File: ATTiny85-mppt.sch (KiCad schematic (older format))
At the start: 49 parts, among them J1 S+, J2 S-, J3 O+, J4 O-, Q1 BUK9511-55A127, Q2 BUK9511-55A127, Q3 2N2222A, Q4 2N2222A, Q5 2N2907A, SW1 Write OP-AMP DIFF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

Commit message: R15 -> 4.7k. Current sensing is more higher than expected. 62mA -> 67mV.
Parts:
- D4, D8, D9: symbol 12f675-mppt-rescue:LED -> ATTiny85-mppt-rescue:LED-12f675-mppt-rescue
- L1, L2: symbol 12f675-mppt-rescue:INDUCTOR -> ATTiny85-mppt-rescue:INDUCTOR-12f675-mppt-rescue
- R15: value 10k -> 4.7k
- SW1: symbol 12f675-mppt-rescue:SW_PUSH -> ATTiny85-mppt-rescue:SW_PUSH-12f675-mppt-rescue
- U2: symbol 12f675-mppt-rescue:LM358N-RESCUE-12f675-mppt -> ATTiny85-mppt-rescue:LM358N-RESCUE-12f675-mppt-12f675-mppt-rescue
- U3: symbol MCU_Microchip_ATtiny:ATtiny85-20PU -> ATTiny85-mppt-rescue:ATtiny85-20PU-MCU_Microchip_ATtiny
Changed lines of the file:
@@
 $EndComp
 $Comp
-L 12f675-mppt-rescue:LM358N-RESCUE-12f675-mppt U2
+L ATTiny85-mppt-rescue:LM358N-RESCUE-12f675-mppt-12f675-mppt-rescue U2
 U 2 1 55C3383E
 P 7500 4850
@@
 $EndComp
 $Comp
-L 12f675-mppt-rescue:INDUCTOR L1
+L ATTiny85-mppt-rescue:INDUCTOR-12f675-mppt-rescue L1
 U 1 1 55C35536
 P 9050 2200
@@
 $EndComp
 $Comp
-L 12f675-mppt-rescue:LED D4
+L ATTiny85-mppt-rescue:LED-12f675-mppt-rescue D4
 U 1 1 55C3BFD1
 P 4550 5300
@@
 Max 25V
 $Comp
-L 12f675-mppt-rescue:LED D9
+L ATTiny85-mppt-rescue:LED-12f675-mppt-rescue D9
 U 1 1 55CCC105
 P 5650 5350
@@
 $EndComp
 $Comp
-L 12f675-mppt-rescue:LED D8
+L ATTiny85-mppt-rescue:LED-12f675-mppt-rescue D8
 U 1 1 55CCC217
 P 5650 4850
@@
 3.6v
 $Comp
-L 12f675-mppt-rescue:LM358N-RESCUE-12f675-mppt U2
+L ATTiny85-mppt-rescue:LM358N-RESCUE-12f675-mppt-12f675-mppt-rescue U2
 U 1 1 56E669E2
 P 8850 4350
@@
 P 9650 4300
 F 0 "R15" V 9730 4300 50  0000 C CNN
-F 1 "10k" V 9650 4300 50  0000 C CNN
+F 1 "4.7k" V 9650 4300 50  0000 C CNN
 F 2 "Resistors_THT:R_Axial_DIN0309_L9.0mm_D3.2mm_P12.70mm_Horizontal" V 9580 4300 50  0001 C CNN
 F 3 "" H 9650 4300 50  0000 C CNN
@@
 	4150 5000 4050 5000
 $Comp
-L 12f675-mppt-rescue:SW_PUSH SW1
+L ATTiny85-mppt-rescue:SW_PUSH-12f675-mppt-rescue SW1
 U 1 1 56ECBA1E
 P 3100 4650
@@
 	2650 4650 2650 5600
 $Comp
-L MCU_Microchip_ATtiny:ATtiny85-20PU U3
+L ATTiny85-mppt-rescue:ATtiny85-20PU-MCU_Microchip_ATtiny U3
 U 1 1 5BC87E53
 P 4450 3400
@@
 	8700 3050 9500 3050
 $Comp
-L 12f675-mppt-rescue:INDUCTOR L2
+L ATTiny85-mppt-rescue:INDUCTOR-12f675-mppt-rescue L2
 U 1 1 5BCF09F4
 P 9050 1850

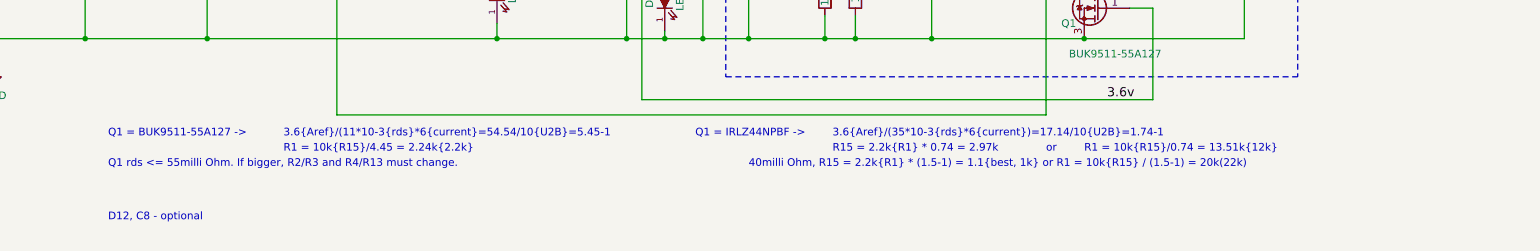
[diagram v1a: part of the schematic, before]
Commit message: refine OP-AMP resistor formula. but it still same with first design(+10mV). it may safe under 3A current.
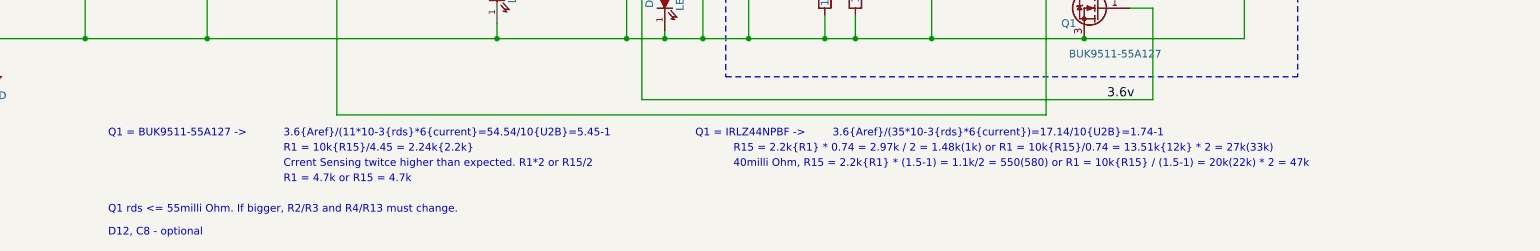
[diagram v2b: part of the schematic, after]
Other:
- note added: "40milli Ohm, R15 = 2.2k{R1} * (1.5-1) = 1.1k/2 = 550(580) or R1 = 10k{R15} / (1.5-1) = 20k(22k) * 2 = 47k"
- note added: "Crrent Sensing twitce higher than expected. R1*2 or R15/2"
- note added: "R1 = 4.7k or R15 = 4.7k"
- note added: "R15 = 2.2k{R1} * 0.74 = 2.97k / 2 = 1.48k(1k) or R1 = 10k{R15}/0.74 = 13.51k{12k} * 2 = 27k(33k)"
- note removed: "40milli Ohm, R15 = 2.2k{R1} * (1.5-1) = 1.1{best, 1k} or R1 = 10k{R15} / (1.5-1) = 20k(22k)"
- note removed: "R1 = 10k{R15}/0.74 = 13.51k{12k}"
- note removed: "R15 = 2.2k{R1} * 0.74 = 2.97k"
- note removed: "or"
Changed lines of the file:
@@
 Text Notes 6750 6250 0    50   ~ 0
 3.6{Aref}/(35*10-3{rds}*6{current})=17.14/10{U2B}=1.74-1
-Text Notes 6750 6350 0    50   ~ 0
-R15 = 2.2k{R1} * 0.74 = 2.97k
-Text Notes 8150 6350 0    50   ~ 0
-or
-Text Notes 8400 6350 0    50   ~ 0
-R1 = 10k{R15}/0.74 = 13.51k{12k}
+Text Notes 6100 6350 0    50   ~ 0
+R15 = 2.2k{R1} * 0.74 = 2.97k / 2 = 1.48k(1k) or R1 = 10k{R15}/0.74 = 13.51k{12k} * 2 = 27k(33k)
 Text Notes 2000 6250 0    50   ~ 0
 Q1 = BUK9511-55A127 ->
@@
 Text Notes 3150 6350 0    50   ~ 0
 R1 = 10k{R15}/4.45 = 2.24k{2.2k}
-Text Notes 6200 6450 0    50   ~ 0
-40milli Ohm, R15 = 2.2k{R1} * (1.5-1) = 1.1{best, 1k} or R1 = 10k{R15} / (1.5-1) = 20k(22k)
-Text Notes 2000 6450 0    50   ~ 0
+Text Notes 6100 6450 0    50   ~ 0
+40milli Ohm, R15 = 2.2k{R1} * (1.5-1) = 1.1k/2 = 550(580) or R1 = 10k{R15} / (1.5-1) = 20k(22k) * 2 = 47k
+Text Notes 2000 6750 0    50   ~ 0
 Q1 rds <= 55milli Ohm. If bigger, R2/R3 and R4/R13 must change.
 $Comp
@@
 Wire Wire Line
 	6600 3100 7250 3100
-Text Notes 2000 6800 0    50   ~ 0
+Text Notes 2000 6900 0    50   ~ 0
 D12, C8 - optional
 Wire Wire Line
@@
 Wire Wire Line
 	4000 4400 5300 4400
+Text Notes 3150 6450 0    50   ~ 0
+Crrent Sensing twitce higher than expected. R1*2 or R15/2
+Text Notes 3150 6550 0    50   ~ 0
+R1 = 4.7k or R15 = 4.7k
 $EndSCHEMATC

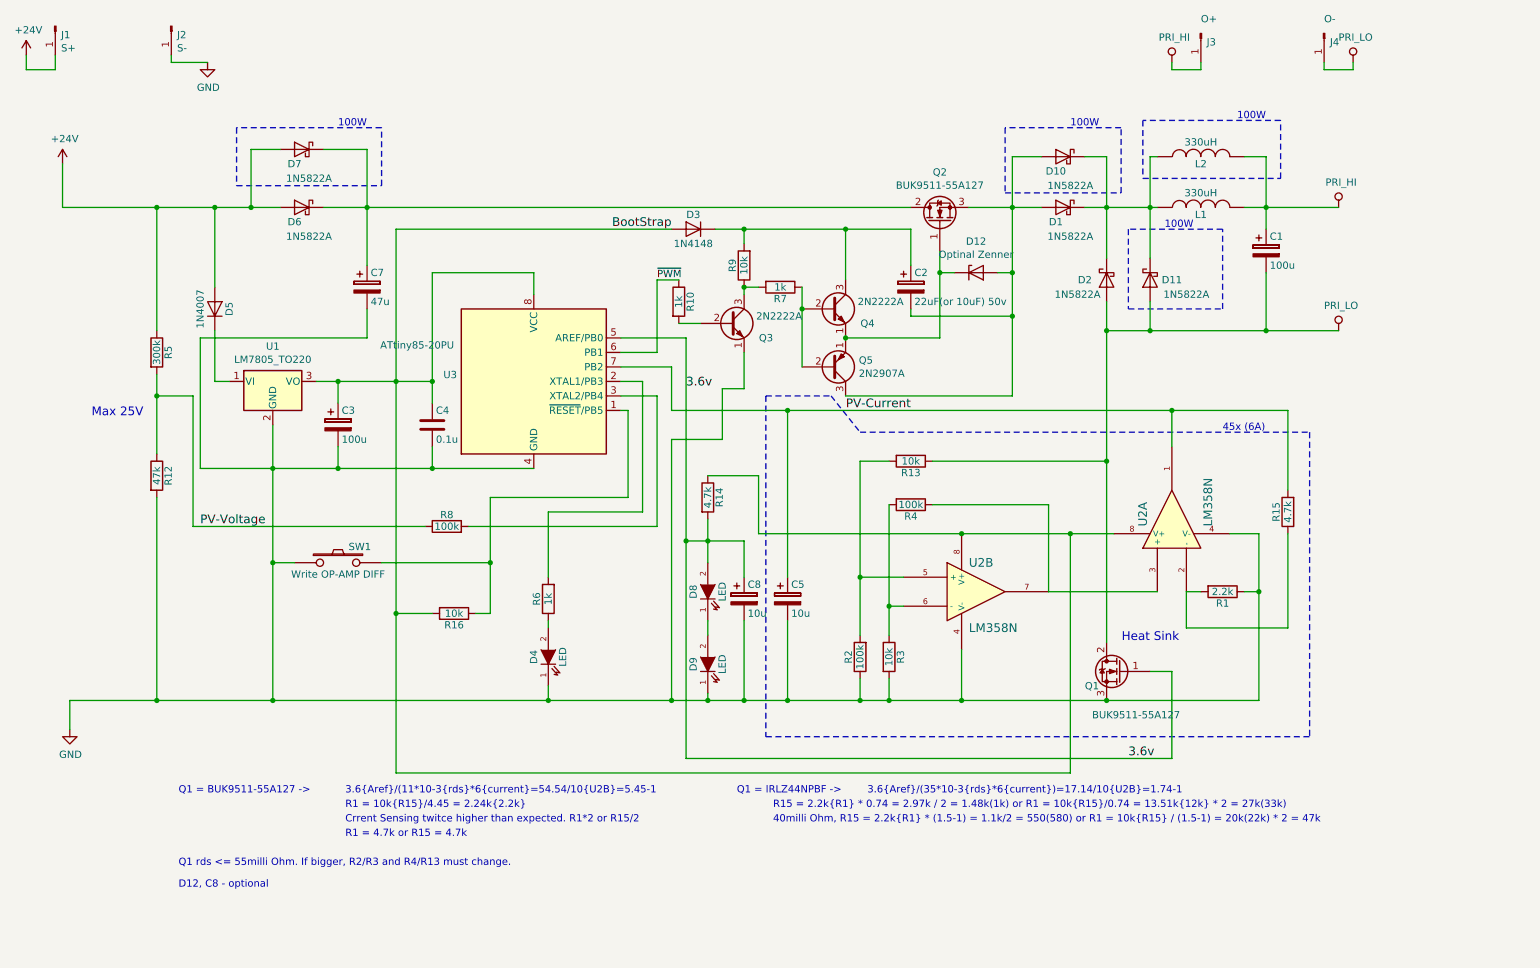
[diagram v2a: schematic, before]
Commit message: update resistor formula.
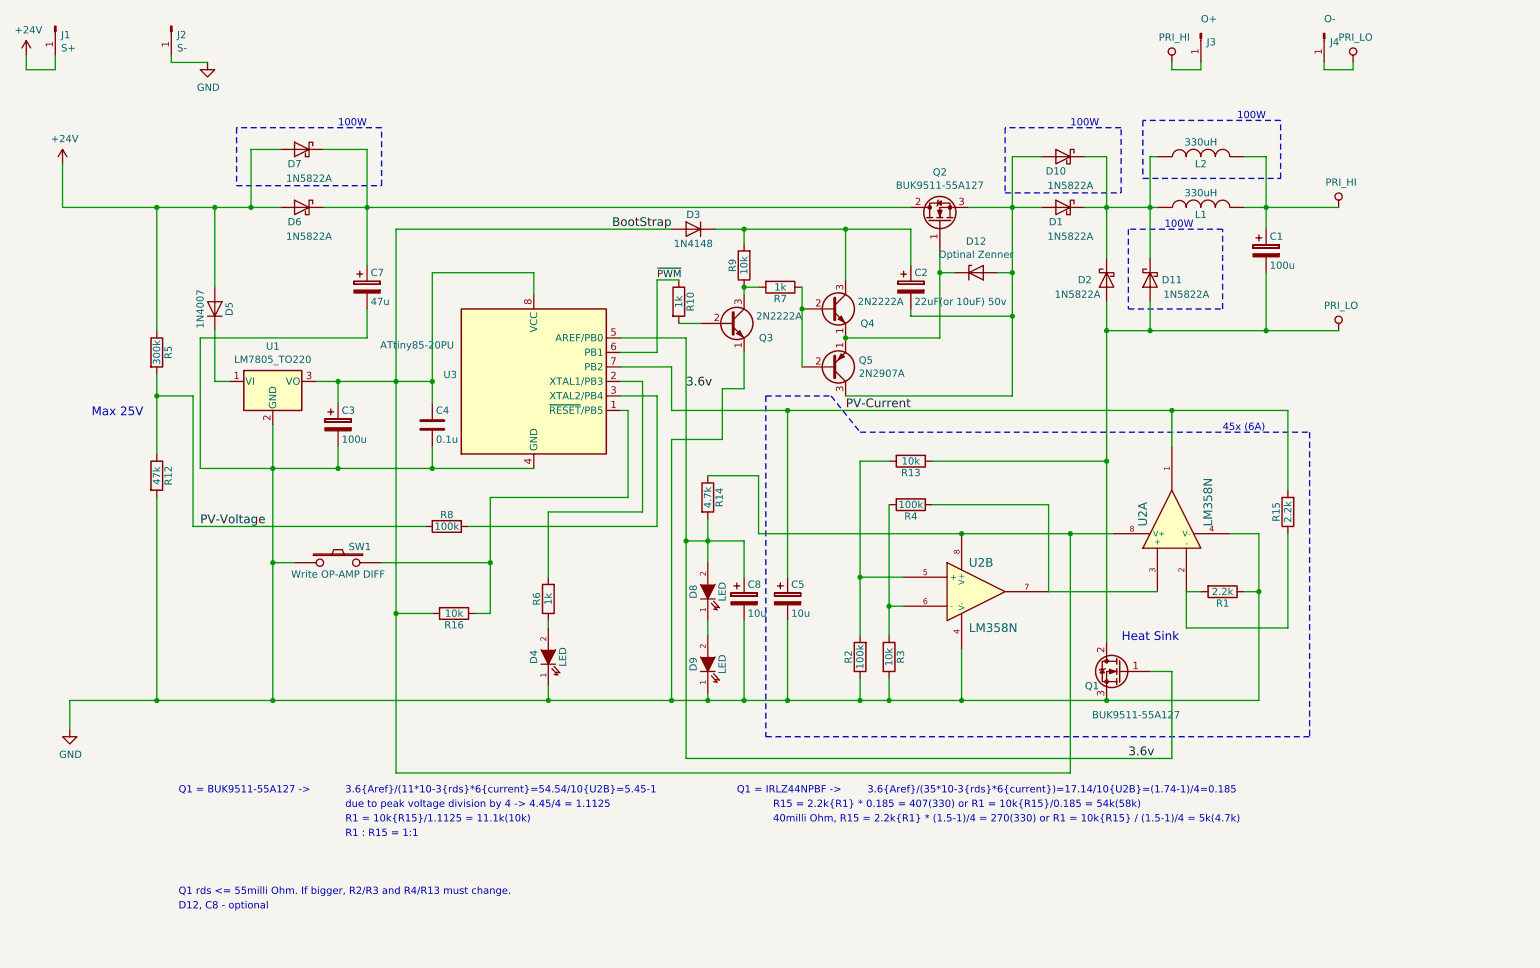
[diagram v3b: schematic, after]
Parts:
- R15: value 4.7k -> 2.2k
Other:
- note added: "3.6{Aref}/(35*10-3{rds}*6{current})=17.14/10{U2B}=(1.74-1)/4=0.185"
- note added: "40milli Ohm, R15 = 2.2k{R1} * (1.5-1)/4 = 270(330) or R1 = 10k{R15} / (1.5-1)/4 = 5k(4.7k)"
- note added: "R1 : R15 = 1:1"
- note added: "R1 = 10k{R15}/1.1125 = 11.1k(10k)"
- note added: "R15 = 2.2k{R1} * 0.185 = 407(330) or R1 = 10k{R15}/0.185 = 54k(58k)"
- note added: "due to peak voltage division by 4 -> 4.45/4 = 1.1125"
- note removed: "3.6{Aref}/(35*10-3{rds}*6{current})=17.14/10{U2B}=1.74-1"
- note removed: "40milli Ohm, R15 = 2.2k{R1} * (1.5-1) = 1.1k/2 = 550(580) or R1 = 10k{R15} / (1.5-1) = 20k(22k) * 2 = 47k"
- note removed: "Crrent Sensing twitce higher than expected. R1*2 or R15/2"
- note removed: "R1 = 10k{R15}/4.45 = 2.24k{2.2k}"
- note removed: "R1 = 4.7k or R15 = 4.7k"
- note removed: "R15 = 2.2k{R1} * 0.74 = 2.97k / 2 = 1.48k(1k) or R1 = 10k{R15}/0.74 = 13.51k{12k} * 2 = 27k(33k)"
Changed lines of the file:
@@
 P 9650 4300
 F 0 "R15" V 9730 4300 50  0000 C CNN
-F 1 "4.7k" V 9650 4300 50  0000 C CNN
+F 1 "2.2k" V 9650 4300 50  0000 C CNN
 F 2 "Resistors_THT:R_Axial_DIN0309_L9.0mm_D3.2mm_P12.70mm_Horizontal" V 9580 4300 50  0001 C CNN
 F 3 "" H 9650 4300 50  0000 C CNN
@@
 Q1 = IRLZ44NPBF ->
 Text Notes 6750 6250 0    50   ~ 0
-3.6{Aref}/(35*10-3{rds}*6{current})=17.14/10{U2B}=1.74-1
+3.6{Aref}/(35*10-3{rds}*6{current})=17.14/10{U2B}=(1.74-1)/4=0.185
 Text Notes 6100 6350 0    50   ~ 0
-R15 = 2.2k{R1} * 0.74 = 2.97k / 2 = 1.48k(1k) or R1 = 10k{R15}/0.74 = 13.51k{12k} * 2 = 27k(33k)
+R15 = 2.2k{R1} * 0.185 = 407(330) or R1 = 10k{R15}/0.185 = 54k(58k)
 Text Notes 2000 6250 0    50   ~ 0
 Q1 = BUK9511-55A127 ->
 Text Notes 3150 6250 0    50   ~ 0
 3.6{Aref}/(11*10-3{rds}*6{current}=54.54/10{U2B}=5.45-1
-Text Notes 3150 6350 0    50   ~ 0
-R1 = 10k{R15}/4.45 = 2.24k{2.2k}
+Text Notes 3150 6450 0    50   ~ 0
+R1 = 10k{R15}/1.1125 = 11.1k(10k)
 Text Notes 6100 6450 0    50   ~ 0
-40milli Ohm, R15 = 2.2k{R1} * (1.5-1) = 1.1k/2 = 550(580) or R1 = 10k{R15} / (1.5-1) = 20k(22k) * 2 = 47k
-Text Notes 2000 6750 0    50   ~ 0
+40milli Ohm, R15 = 2.2k{R1} * (1.5-1)/4 = 270(330) or R1 = 10k{R15} / (1.5-1)/4 = 5k(4.7k)
+Text Notes 2000 6950 0    50   ~ 0
 Q1 rds <= 55milli Ohm. If bigger, R2/R3 and R4/R13 must change.
 $Comp
@@
 Wire Wire Line
 	6600 3100 7250 3100
-Text Notes 2000 6900 0    50   ~ 0
+Text Notes 2000 7050 0    50   ~ 0
 D12, C8 - optional
 Wire Wire Line
@@
 Wire Wire Line
 	4000 4400 5300 4400
-Text Notes 3150 6450 0    50   ~ 0
-Crrent Sensing twitce higher than expected. R1*2 or R15/2
+Text Notes 3150 6350 0    50   ~ 0
+due to peak voltage division by 4 -> 4.45/4 = 1.1125
 Text Notes 3150 6550 0    50   ~ 0
-R1 = 4.7k or R15 = 4.7k
+R1 : R15 = 1:1
 $EndSCHEMATC

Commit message: add note for R15.
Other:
- note added: "20x (6A)"
- note added: "R15\n6A = 2.2k, 3A = 4.7k"
- note removed: "45x (6A)"
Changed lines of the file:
@@
 	9200 2350 8550 2350
 Text Notes 9200 3750 0    50   ~ 0
-45x (6A)
+20x (6A)
 Text Notes 3100 1650 0    50   ~ 0
 100W
@@
 Text Notes 3150 6550 0    50   ~ 0
 R1 : R15 = 1:1
+Text Notes 9850 4350 0    50   ~ 0
+R15\n6A = 2.2k, 3A = 4.7k
 $EndSCHEMATC

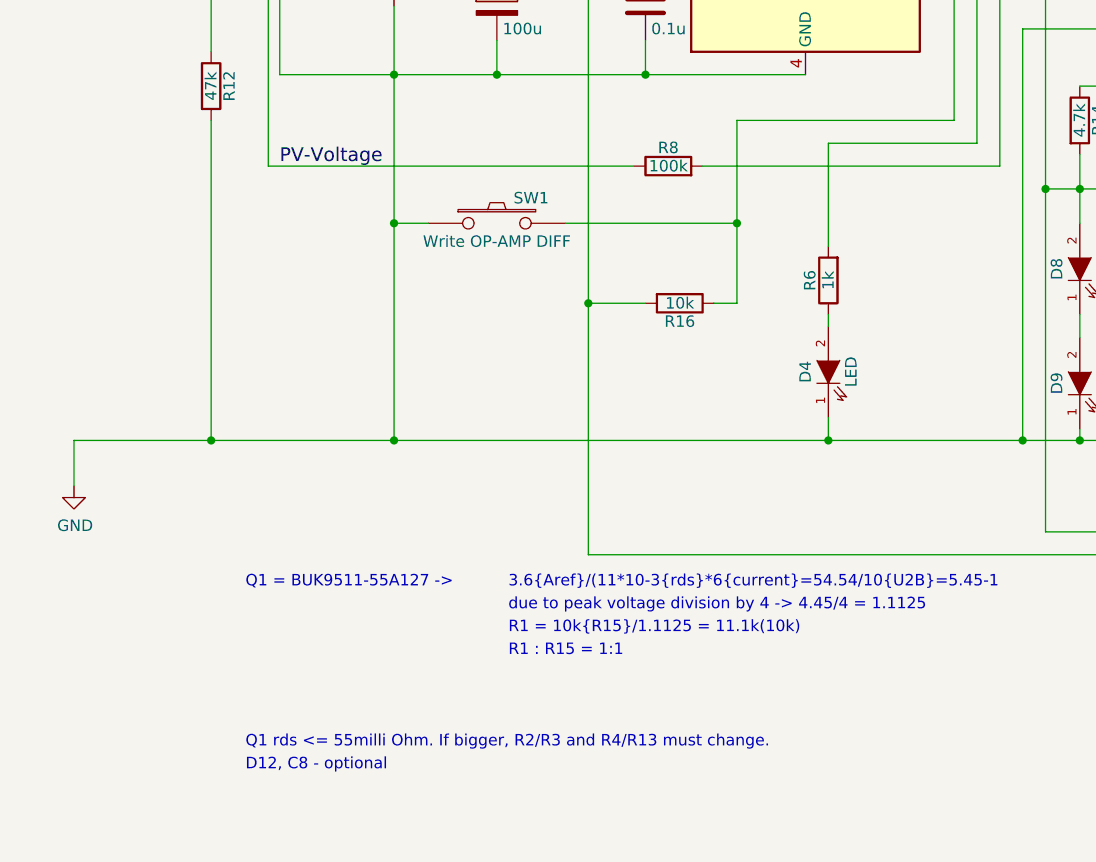
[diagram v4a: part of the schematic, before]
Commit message: Add voltage clamp.
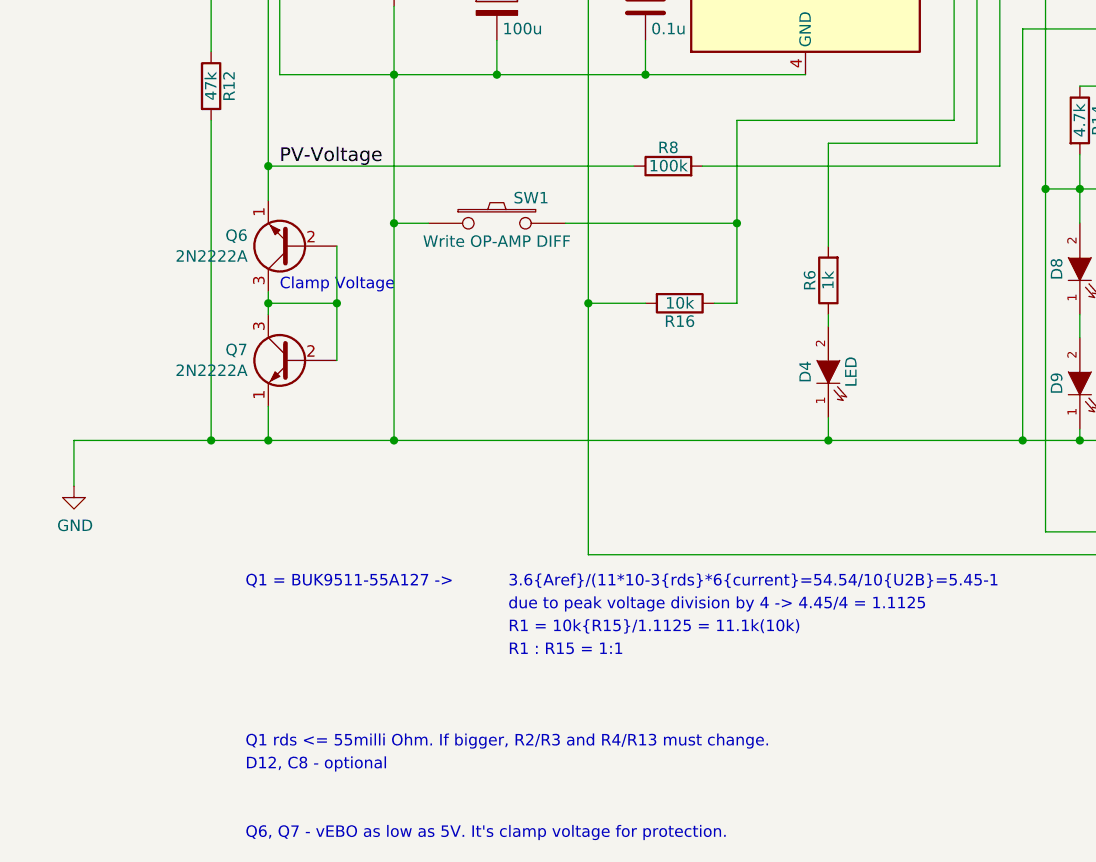
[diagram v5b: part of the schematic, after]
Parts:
- added Q6, Q7: 2N2222A, TO_SOT_Packages_THT:TO-92_Inline_Wide, symbol Device:Q_NPN_EBC
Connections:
- net GND: now also Q7.1 (E)
- net PV-Voltage: now also Q6.1 (E)
- new net: Q6.2 (B), Q6.3 (C), Q7.2 (B), Q7.3 (C)
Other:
- note added: "Clamp Voltage"
- note added: "Q6, Q7 - vEBO as low as 5V. It's clamp voltage for protection."
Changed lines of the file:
@@
 Sheet 1 1
 Title "Simple MPPT with ATTiny85"
-Date "2018-12-17"
-Rev "1.8"
+Date "2018-12-26"
+Rev "1.9"
 Comp ""
 Comment1 ""
@@
 	2250 2200 2500 2200
 Wire Wire Line
-	2650 5600 1850 5600
+	2650 5600 2100 5600
 Wire Wire Line
 	1850 2200 2250 2200
@@
 Text Notes 9850 4350 0    50   ~ 0
 R15\n6A = 2.2k, 3A = 4.7k
+$Comp
+L Device:Q_NPN_EBC Q6
+U 1 1 5C237CD3
+P 2200 4750
+F 0 "Q6" H 2390 4704 50  0000 L CNN
+F 1 "2N2222A" H 2390 4795 50  0000 L CNN
+F 2 "TO_SOT_Packages_THT:TO-92_Inline_Wide" H 2400 4850 50  0001 C CNN
+F 3 "~" H 2200 4750 50  0001 C CNN
+	1    2200 4750
+	-1   0    0    1
+$EndComp
+$Comp
+L Device:Q_NPN_EBC Q7
+U 1 1 5C237FCB
+P 2200 5250
+F 0 "Q7" H 2390 5296 50  0000 L CNN
+F 1 "2N2222A" H 2390 5205 50  0000 L CNN
+F 2 "TO_SOT_Packages_THT:TO-92_Inline_Wide" H 2400 5350 50  0001 C CNN
+F 3 "~" H 2200 5250 50  0001 C CNN
+	1    2200 5250
+	-1   0    0    -1
+$EndComp
+Wire Wire Line
+	2100 4550 2100 4400
+Connection ~ 2100 4400
+Wire Wire Line
+	2100 4950 2100 5000
+Wire Wire Line
+	2100 5450 2100 5600
+Connection ~ 2100 5600
+Wire Wire Line
+	2100 5600 1850 5600
+Wire Wire Line
+	2400 4750 2400 5000
+Wire Wire Line
+	2400 5000 2100 5000
+Connection ~ 2400 5000
+Wire Wire Line
+	2400 5000 2400 5250
+Connection ~ 2100 5000
+Wire Wire Line
+	2100 5000 2100 5050
+Text Notes 2150 4950 0    50   ~ 0
+Clamp Voltage
+Text Notes 2000 7350 0    50   ~ 0
+Q6, Q7 - vEBO as low as 5V. It's clamp voltage for protection.
 $EndSCHEMATC
